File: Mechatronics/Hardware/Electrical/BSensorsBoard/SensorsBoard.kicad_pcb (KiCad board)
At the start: 2 copper layers, 49.8 x 13.7 mm, 10 parts, among them J1 Conn_01x01_Male, J2 Conn_01x01_Male, J3 Conn_01x01_Male, J4 Conn_01x01_Male, J5 Conn_01x01_Male, J6 Conn_01x01_Male, J7 Conn_01x01_Male, J8 Conn_01x01_Male, U1 ITR1802, U2 ITR1802

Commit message: Added changes
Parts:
- removed J5, J6, J7, J8: Conn_01x01_Male, Encoder:No3dmodelPinHeader_1x01_P2.54mm_Vertical
- removed U2: ITR1802, Encoder:itr8102
- added J1: Conn_01x01_Male, Encoder:No3dmodelPinHeader_1x01_P2.54mm_Vertical, F.Cu at (150.7, 120.2)
- added J1: Conn_01x01_Male, Encoder:No3dmodelPinHeader_1x01_P2.54mm_Vertical, F.Cu at (109.3, 76.7)
- added J1: Conn_01x01_Male, Encoder:No3dmodelPinHeader_1x01_P2.54mm_Vertical, F.Cu at (126.8, 92.9)
- added J1: Conn_01x01_Male, Encoder:No3dmodelPinHeader_1x01_P2.54mm_Vertical, F.Cu at (102.9, 92.9)
- added J1: Conn_01x01_Male, Encoder:No3dmodelPinHeader_1x01_P2.54mm_Vertical, F.Cu at (109.2, 104.0)
- added J1: Conn_01x01_Male, Encoder:No3dmodelPinHeader_1x01_P2.54mm_Vertical, F.Cu at (133.2, 104.0)
- added J1: Conn_01x01_Male, Encoder:No3dmodelPinHeader_1x01_P2.54mm_Vertical, F.Cu at (126.7, 120.2)
- added J1: Conn_01x01_Male, Encoder:No3dmodelPinHeader_1x01_P2.54mm_Vertical, F.Cu at (174.7, 120.2)
- added J1: Conn_01x01_Male, Encoder:No3dmodelPinHeader_1x01_P2.54mm_Vertical, F.Cu at (157.1, 104.0)
- added J1: Conn_01x01_Male, Encoder:No3dmodelPinHeader_1x01_P2.54mm_Vertical, F.Cu at (181.1, 104.0)
- added J1: Conn_01x01_Male, Encoder:No3dmodelPinHeader_1x01_P2.54mm_Vertical, F.Cu at (150.8, 92.9)
- added J1: Conn_01x01_Male, Encoder:No3dmodelPinHeader_1x01_P2.54mm_Vertical, F.Cu at (174.7, 92.9)
- added J1: Conn_01x01_Male, Encoder:No3dmodelPinHeader_1x01_P2.54mm_Vertical, F.Cu at (157.2, 76.7)
- added J1: Conn_01x01_Male, Encoder:No3dmodelPinHeader_1x01_P2.54mm_Vertical, F.Cu at (181.2, 76.7)
- added J1: Conn_01x01_Male, Encoder:No3dmodelPinHeader_1x01_P2.54mm_Vertical, F.Cu at (133.2, 76.7)
- added J2: Conn_01x01_Male, Encoder:No3dmodelPinHeader_1x01_P2.54mm_Vertical, F.Cu at (150.8, 96.4)
- added J2: Conn_01x01_Male, Encoder:No3dmodelPinHeader_1x01_P2.54mm_Vertical, F.Cu at (102.9, 96.4)
- added J2: Conn_01x01_Male, Encoder:No3dmodelPinHeader_1x01_P2.54mm_Vertical, F.Cu at (133.2, 73.2)
- added J2: Conn_01x01_Male, Encoder:No3dmodelPinHeader_1x01_P2.54mm_Vertical, F.Cu at (126.8, 96.4)
- added J2: Conn_01x01_Male, Encoder:No3dmodelPinHeader_1x01_P2.54mm_Vertical, F.Cu at (109.2, 100.5)
- added J2: Conn_01x01_Male, Encoder:No3dmodelPinHeader_1x01_P2.54mm_Vertical, F.Cu at (133.2, 100.5)
- added J2: Conn_01x01_Male, Encoder:No3dmodelPinHeader_1x01_P2.54mm_Vertical, F.Cu at (126.7, 123.7)
- added J2: Conn_01x01_Male, Encoder:No3dmodelPinHeader_1x01_P2.54mm_Vertical, F.Cu at (174.7, 123.7)
- added J2: Conn_01x01_Male, Encoder:No3dmodelPinHeader_1x01_P2.54mm_Vertical, F.Cu at (181.1, 100.5)
- added J2: Conn_01x01_Male, Encoder:No3dmodelPinHeader_1x01_P2.54mm_Vertical, F.Cu at (150.7, 123.7)
- added J2: Conn_01x01_Male, Encoder:No3dmodelPinHeader_1x01_P2.54mm_Vertical, F.Cu at (157.1, 100.5)
- added J2: Conn_01x01_Male, Encoder:No3dmodelPinHeader_1x01_P2.54mm_Vertical, F.Cu at (157.2, 73.2)
- added J2: Conn_01x01_Male, Encoder:No3dmodelPinHeader_1x01_P2.54mm_Vertical, F.Cu at (181.2, 73.2)
- added J2: Conn_01x01_Male, Encoder:No3dmodelPinHeader_1x01_P2.54mm_Vertical, F.Cu at (174.7, 96.4)
- added J2: Conn_01x01_Male, Encoder:No3dmodelPinHeader_1x01_P2.54mm_Vertical, F.Cu at (109.3, 73.2)
- added J3: Conn_01x01_Male, Encoder:No3dmodelPinHeader_1x01_P2.54mm_Vertical, F.Cu at (150.7, 76.8)
- added J3: Conn_01x01_Male, Encoder:No3dmodelPinHeader_1x01_P2.54mm_Vertical, F.Cu at (109.3, 92.8)
- added J3: Conn_01x01_Male, Encoder:No3dmodelPinHeader_1x01_P2.54mm_Vertical, F.Cu at (102.8, 76.8)
- added J3: Conn_01x01_Male, Encoder:No3dmodelPinHeader_1x01_P2.54mm_Vertical, F.Cu at (133.3, 92.8)
- added J3: Conn_01x01_Male, Encoder:No3dmodelPinHeader_1x01_P2.54mm_Vertical, F.Cu at (126.7, 104.1)
- added J3: Conn_01x01_Male, Encoder:No3dmodelPinHeader_1x01_P2.54mm_Vertical, F.Cu at (102.8, 104.1)
- added J3: Conn_01x01_Male, Encoder:No3dmodelPinHeader_1x01_P2.54mm_Vertical, F.Cu at (133.2, 120.1)
- added J3: Conn_01x01_Male, Encoder:No3dmodelPinHeader_1x01_P2.54mm_Vertical, F.Cu at (157.1, 120.1)
- added J3: Conn_01x01_Male, Encoder:No3dmodelPinHeader_1x01_P2.54mm_Vertical, F.Cu at (181.2, 92.8)
- added J3: Conn_01x01_Male, Encoder:No3dmodelPinHeader_1x01_P2.54mm_Vertical, F.Cu at (174.6, 104.1)
- added J3: Conn_01x01_Male, Encoder:No3dmodelPinHeader_1x01_P2.54mm_Vertical, F.Cu at (181.1, 120.1)
- added J3: Conn_01x01_Male, Encoder:No3dmodelPinHeader_1x01_P2.54mm_Vertical, F.Cu at (150.7, 104.1)
- added J3: Conn_01x01_Male, Encoder:No3dmodelPinHeader_1x01_P2.54mm_Vertical, F.Cu at (157.2, 92.8)
- added J3: Conn_01x01_Male, Encoder:No3dmodelPinHeader_1x01_P2.54mm_Vertical, F.Cu at (174.7, 76.8)
- added J3: Conn_01x01_Male, Encoder:No3dmodelPinHeader_1x01_P2.54mm_Vertical, F.Cu at (126.8, 76.8)
- added J4: Conn_01x01_Male, Encoder:No3dmodelPinHeader_1x01_P2.54mm_Vertical, F.Cu at (150.7, 73.2)
- added J4: Conn_01x01_Male, Encoder:No3dmodelPinHeader_1x01_P2.54mm_Vertical, F.Cu at (126.8, 73.2)
- added J4: Conn_01x01_Male, Encoder:No3dmodelPinHeader_1x01_P2.54mm_Vertical, F.Cu at (102.8, 73.2)
- added J4: Conn_01x01_Male, Encoder:No3dmodelPinHeader_1x01_P2.54mm_Vertical, F.Cu at (133.3, 96.4)
- added J4: Conn_01x01_Male, Encoder:No3dmodelPinHeader_1x01_P2.54mm_Vertical, F.Cu at (126.7, 100.5)
- added J4: Conn_01x01_Male, Encoder:No3dmodelPinHeader_1x01_P2.54mm_Vertical, F.Cu at (102.8, 100.5)
- added J4: Conn_01x01_Male, Encoder:No3dmodelPinHeader_1x01_P2.54mm_Vertical, F.Cu at (133.2, 123.7)
- added J4: Conn_01x01_Male, Encoder:No3dmodelPinHeader_1x01_P2.54mm_Vertical, F.Cu at (174.6, 100.5)
- added J4: Conn_01x01_Male, Encoder:No3dmodelPinHeader_1x01_P2.54mm_Vertical, F.Cu at (157.1, 123.7)
- added J4: Conn_01x01_Male, Encoder:No3dmodelPinHeader_1x01_P2.54mm_Vertical, F.Cu at (181.1, 123.7)
- added J4: Conn_01x01_Male, Encoder:No3dmodelPinHeader_1x01_P2.54mm_Vertical, F.Cu at (174.7, 73.2)
- added J4: Conn_01x01_Male, Encoder:No3dmodelPinHeader_1x01_P2.54mm_Vertical, F.Cu at (181.2, 96.4)
- added J4: Conn_01x01_Male, Encoder:No3dmodelPinHeader_1x01_P2.54mm_Vertical, F.Cu at (157.2, 96.4)
- added J4: Conn_01x01_Male, Encoder:No3dmodelPinHeader_1x01_P2.54mm_Vertical, F.Cu at (150.7, 100.5)
- added J4: Conn_01x01_Male, Encoder:No3dmodelPinHeader_1x01_P2.54mm_Vertical, F.Cu at (109.3, 96.4)
- added U1: ITR1802, Encoder:itr8102, F.Cu at (154.0, 87.8)
- added U1: ITR1802, Encoder:itr8102, F.Cu at (130.1, 81.8)
- added U1: ITR1802, Encoder:itr8102, F.Cu at (106.1, 81.8)
- added U1: ITR1802, Encoder:itr8102, F.Cu at (130.0, 87.8)
- added U1: ITR1802, Encoder:itr8102, F.Cu at (130.0, 109.1)
- added U1: ITR1802, Encoder:itr8102, F.Cu at (106.0, 109.1)
- added U1: ITR1802, Encoder:itr8102, F.Cu at (129.9, 115.1)
- added U1: ITR1802, Encoder:itr8102, F.Cu at (154.0, 81.8)
- added U1: ITR1802, Encoder:itr8102, F.Cu at (178.0, 81.8)
- added U1: ITR1802, Encoder:itr8102, F.Cu at (177.9, 87.8)
- added U1: ITR1802, Encoder:itr8102, F.Cu at (177.9, 109.1)
- added U1: ITR1802, Encoder:itr8102, F.Cu at (153.9, 115.1)
- added U1: ITR1802, Encoder:itr8102, F.Cu at (177.8, 115.1)
- added U1: ITR1802, Encoder:itr8102, F.Cu at (153.9, 109.1)
- added U1: ITR1802, Encoder:itr8102, F.Cu at (106.1, 87.8)
- moved J1 54.5 mm to (102.8, 120.2)
- moved J3 54.5 mm to (109.2, 120.1)
- moved U1 54.5 mm to (106.0, 115.1)
- moved J2 54.5 mm to (102.8, 123.7)
- moved J4 54.5 mm to (109.2, 123.7)
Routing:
- net (no net): track 0.00 -> 534.2 mm
- net Net-(J5-Pad1): track 9.53 -> 0.00 mm
- net Net-(J6-Pad1): track 9.22 -> 0.00 mm
- net Net-(J8-Pad1): track 9.10 -> 0.00 mm
- net Net-(J7-Pad1): track 8.42 -> 0.00 mm
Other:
- board size 49.8 x 13.7 mm -> 95.9 x 54.7 mm
- board text removed: "A"
- board text removed: "B"

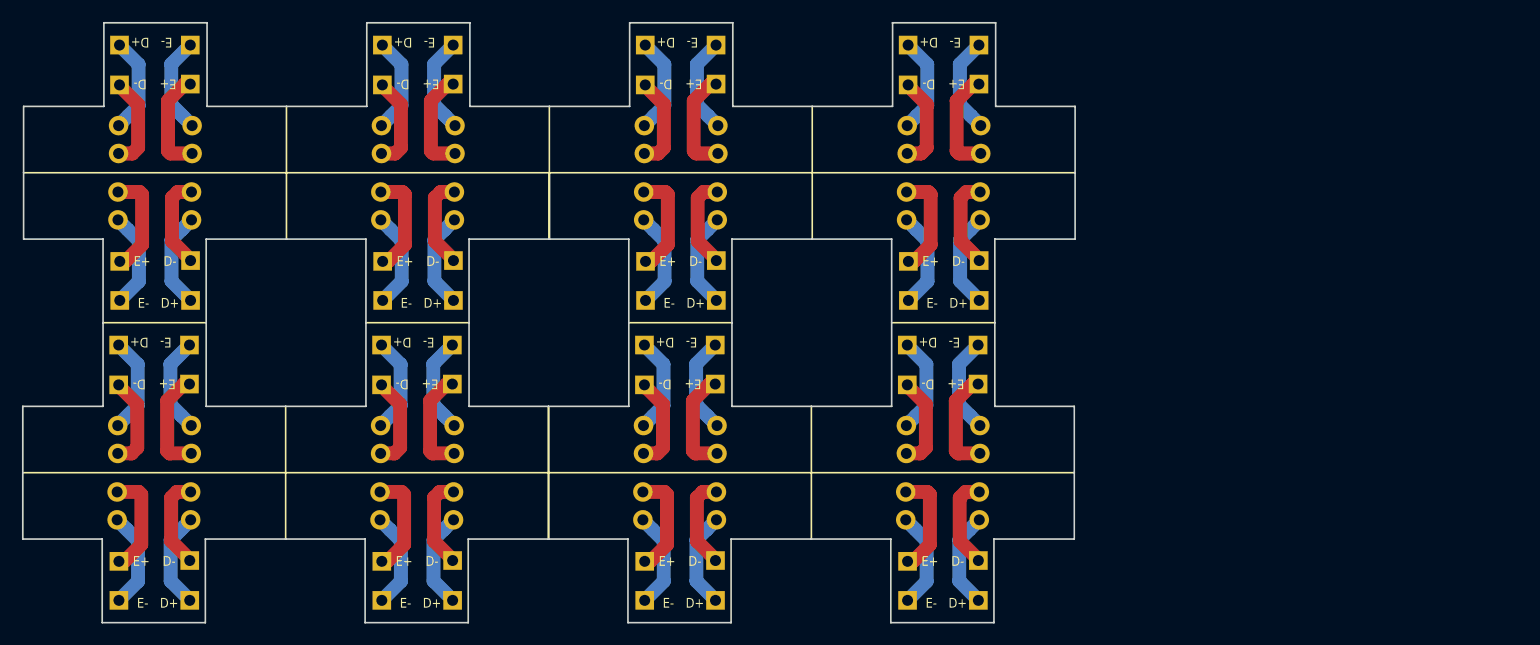
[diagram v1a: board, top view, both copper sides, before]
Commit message: Added SensorsBoard Gerbers
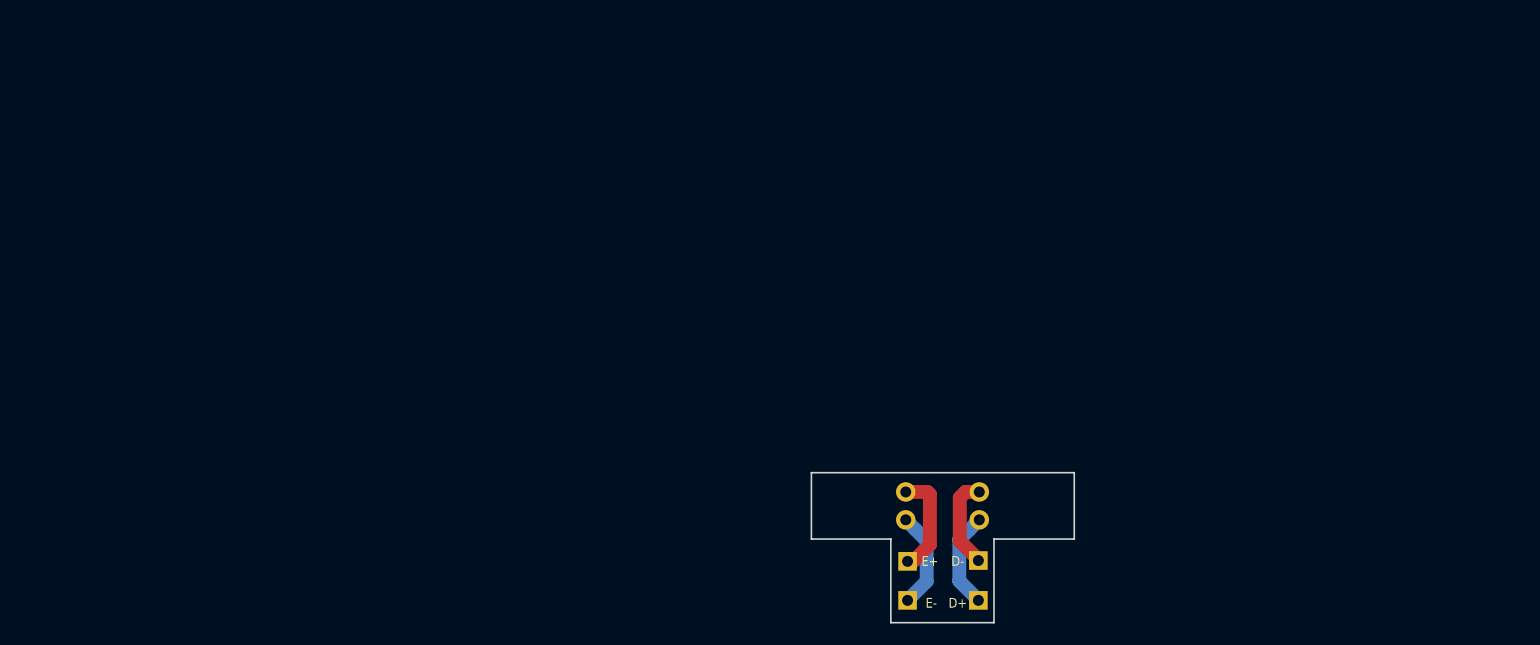
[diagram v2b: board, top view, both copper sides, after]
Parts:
- removed the J1 at (150.7, 120.2)
- removed the J1 at (109.3, 76.7)
- removed the J1 at (126.8, 92.9)
- removed the J1 at (102.9, 92.9)
- removed the J1 at (109.2, 104.0)
- removed the J1 at (133.2, 104.0)
- removed the J1 at (126.7, 120.2)
- removed the J1 at (102.8, 120.2)
- removed the J1 at (157.1, 104.0)
- removed the J1 at (181.1, 104.0)
- removed the J1 at (150.8, 92.9)
- removed the J1 at (174.7, 92.9)
- removed the J1 at (157.2, 76.7)
- removed the J1 at (181.2, 76.7)
- removed the J1 at (133.2, 76.7)
- removed the J2 at (150.8, 96.4)
- removed the J2 at (102.9, 96.4)
- removed the J2 at (133.2, 73.2)
- removed the J2 at (126.8, 96.4)
- removed the J2 at (109.2, 100.5)
- removed the J2 at (133.2, 100.5)
- removed the J2 at (126.7, 123.7)
- removed the J2 at (102.8, 123.7)
- removed the J2 at (181.1, 100.5)
- removed the J2 at (150.7, 123.7)
- removed the J2 at (157.1, 100.5)
- removed the J2 at (157.2, 73.2)
- removed the J2 at (181.2, 73.2)
- removed the J2 at (174.7, 96.4)
- removed the J2 at (109.3, 73.2)
- removed the J3 at (150.7, 76.8)
- removed the J3 at (109.3, 92.8)
- removed the J3 at (102.8, 76.8)
- removed the J3 at (133.3, 92.8)
- removed the J3 at (126.7, 104.1)
- removed the J3 at (102.8, 104.1)
- removed the J3 at (133.2, 120.1)
- removed the J3 at (109.2, 120.1)
- removed the J3 at (157.1, 120.1)
- removed the J3 at (181.2, 92.8)
- removed the J3 at (174.6, 104.1)
- removed the J3 at (150.7, 104.1)
- removed the J3 at (157.2, 92.8)
- removed the J3 at (174.7, 76.8)
- removed the J3 at (126.8, 76.8)
- removed the J4 at (150.7, 73.2)
- removed the J4 at (126.8, 73.2)
- removed the J4 at (102.8, 73.2)
- removed the J4 at (133.3, 96.4)
- removed the J4 at (126.7, 100.5)
- removed the J4 at (102.8, 100.5)
- removed the J4 at (133.2, 123.7)
- removed the J4 at (109.2, 123.7)
- removed the J4 at (174.6, 100.5)
- removed the J4 at (157.1, 123.7)
- removed the J4 at (174.7, 73.2)
- removed the J4 at (181.2, 96.4)
- removed the J4 at (157.2, 96.4)
- removed the J4 at (150.7, 100.5)
- removed the J4 at (109.3, 96.4)
- removed the U1 at (154.0, 87.8)
- removed the U1 at (130.1, 81.8)
- removed the U1 at (106.1, 81.8)
- removed the U1 at (130.0, 87.8)
- removed the U1 at (130.0, 109.1)
- removed the U1 at (106.0, 109.1)
- removed the U1 at (129.9, 115.1)
- removed the U1 at (106.0, 115.1)
- removed the U1 at (154.0, 81.8)
- removed the U1 at (178.0, 81.8)
- removed the U1 at (177.9, 87.8)
- removed the U1 at (177.9, 109.1)
- removed the U1 at (153.9, 115.1)
- removed the U1 at (153.9, 109.1)
- removed the U1 at (106.1, 87.8)
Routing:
- net (no net): track 534.2 -> 35.6 mm
- net Net-(J1-Pad1): track 9.53 -> 0.00 mm
- net Net-(J2-Pad1): track 8.85 -> 0.00 mm
- net Net-(J4-Pad1): track 8.81 -> 0.00 mm
- net Net-(J3-Pad1): track 8.42 -> 0.00 mm
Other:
- board size 95.9 x 54.7 mm -> 24 x 13.7 mm

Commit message: Changes
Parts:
- added J1: Conn_01x01_Male, Encoder:No3dmodelPinHeader_1x01_P2.54mm_Vertical, F.Cu at (222.3, 120.2)
- added J1: Conn_01x01_Male, Encoder:No3dmodelPinHeader_1x01_P2.54mm_Vertical, F.Cu at (228.7, 100.0)
- added J1: Conn_01x01_Male, Encoder:No3dmodelPinHeader_1x01_P2.54mm_Vertical, F.Cu at (210.4, 120.2)
- added J1: Conn_01x01_Male, Encoder:No3dmodelPinHeader_1x01_P2.54mm_Vertical, F.Cu at (216.7, 100.0)
- added J1: Conn_01x01_Male, Encoder:No3dmodelPinHeader_1x01_P2.54mm_Vertical, F.Cu at (198.5, 120.2)
- added J1: Conn_01x01_Male, Encoder:No3dmodelPinHeader_1x01_P2.54mm_Vertical, F.Cu at (204.8, 100.0)
- added J1: Conn_01x01_Male, Encoder:No3dmodelPinHeader_1x01_P2.54mm_Vertical, F.Cu at (186.6, 120.2)
- added J1: Conn_01x01_Male, Encoder:No3dmodelPinHeader_1x01_P2.54mm_Vertical, F.Cu at (192.9, 100.0)
- added J1: Conn_01x01_Male, Encoder:No3dmodelPinHeader_1x01_P2.54mm_Vertical, F.Cu at (181.0, 100.0)
- added J2: Conn_01x01_Male, Encoder:No3dmodelPinHeader_1x01_P2.54mm_Vertical, F.Cu at (228.7, 96.5)
- added J2: Conn_01x01_Male, Encoder:No3dmodelPinHeader_1x01_P2.54mm_Vertical, F.Cu at (222.3, 123.7)
- added J2: Conn_01x01_Male, Encoder:No3dmodelPinHeader_1x01_P2.54mm_Vertical, F.Cu at (216.7, 96.5)
- added J2: Conn_01x01_Male, Encoder:No3dmodelPinHeader_1x01_P2.54mm_Vertical, F.Cu at (210.4, 123.7)
- added J2: Conn_01x01_Male, Encoder:No3dmodelPinHeader_1x01_P2.54mm_Vertical, F.Cu at (204.8, 96.5)
- added J2: Conn_01x01_Male, Encoder:No3dmodelPinHeader_1x01_P2.54mm_Vertical, F.Cu at (198.5, 123.7)
- added J2: Conn_01x01_Male, Encoder:No3dmodelPinHeader_1x01_P2.54mm_Vertical, F.Cu at (186.6, 123.7)
- added J2: Conn_01x01_Male, Encoder:No3dmodelPinHeader_1x01_P2.54mm_Vertical, F.Cu at (192.9, 96.5)
- added J2: Conn_01x01_Male, Encoder:No3dmodelPinHeader_1x01_P2.54mm_Vertical, F.Cu at (181.0, 96.5)
- added J3: Conn_01x01_Male, Encoder:No3dmodelPinHeader_1x01_P2.54mm_Vertical, F.Cu at (222.2, 100.1)
- added J3: Conn_01x01_Male, Encoder:No3dmodelPinHeader_1x01_P2.54mm_Vertical, F.Cu at (228.8, 120.1)
- added J3: Conn_01x01_Male, Encoder:No3dmodelPinHeader_1x01_P2.54mm_Vertical, F.Cu at (210.3, 100.1)
- added J3: Conn_01x01_Male, Encoder:No3dmodelPinHeader_1x01_P2.54mm_Vertical, F.Cu at (216.8, 120.1)
- added J3: Conn_01x01_Male, Encoder:No3dmodelPinHeader_1x01_P2.54mm_Vertical, F.Cu at (198.4, 100.1)
- added J3: Conn_01x01_Male, Encoder:No3dmodelPinHeader_1x01_P2.54mm_Vertical, F.Cu at (204.9, 120.1)
- added J3: Conn_01x01_Male, Encoder:No3dmodelPinHeader_1x01_P2.54mm_Vertical, F.Cu at (186.5, 100.1)
- added J3: Conn_01x01_Male, Encoder:No3dmodelPinHeader_1x01_P2.54mm_Vertical, F.Cu at (193.0, 120.1)
- added J3: Conn_01x01_Male, Encoder:No3dmodelPinHeader_1x01_P2.54mm_Vertical, F.Cu at (174.5, 100.1)
- added J4: Conn_01x01_Male, Encoder:No3dmodelPinHeader_1x01_P2.54mm_Vertical, F.Cu at (228.8, 123.7)
- added J4: Conn_01x01_Male, Encoder:No3dmodelPinHeader_1x01_P2.54mm_Vertical, F.Cu at (222.2, 96.5)
- added J4: Conn_01x01_Male, Encoder:No3dmodelPinHeader_1x01_P2.54mm_Vertical, F.Cu at (216.8, 123.7)
- added J4: Conn_01x01_Male, Encoder:No3dmodelPinHeader_1x01_P2.54mm_Vertical, F.Cu at (210.3, 96.5)
- added J4: Conn_01x01_Male, Encoder:No3dmodelPinHeader_1x01_P2.54mm_Vertical, F.Cu at (204.9, 123.7)
- added J4: Conn_01x01_Male, Encoder:No3dmodelPinHeader_1x01_P2.54mm_Vertical, F.Cu at (198.4, 96.5)
- added J4: Conn_01x01_Male, Encoder:No3dmodelPinHeader_1x01_P2.54mm_Vertical, F.Cu at (186.5, 96.5)
- added J4: Conn_01x01_Male, Encoder:No3dmodelPinHeader_1x01_P2.54mm_Vertical, F.Cu at (193.0, 123.7)
- added J4: Conn_01x01_Male, Encoder:No3dmodelPinHeader_1x01_P2.54mm_Vertical, F.Cu at (174.5, 96.5)
- added U1: ITR1802, Encoder:itr8102, F.Cu at (225.5, 115.1)
- added U1: ITR1802, Encoder:itr8102, F.Cu at (225.5, 105.1)
- added U1: ITR1802, Encoder:itr8102, F.Cu at (213.6, 115.1)
- added U1: ITR1802, Encoder:itr8102, F.Cu at (213.6, 105.1)
- added U1: ITR1802, Encoder:itr8102, F.Cu at (201.7, 115.1)
- added U1: ITR1802, Encoder:itr8102, F.Cu at (201.6, 105.1)
- added U1: ITR1802, Encoder:itr8102, F.Cu at (189.7, 105.1)
- added U1: ITR1802, Encoder:itr8102, F.Cu at (189.7, 115.1)
- added U1: ITR1802, Encoder:itr8102, F.Cu at (177.8, 105.1)
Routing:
- net (no net): track 35.6 -> 356.1 mm
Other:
- board size 24 x 13.7 mm -> 57 x 31.3 mm

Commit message: Changes
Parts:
- removed the J1 at (222.3, 120.2)
- removed the J1 at (228.7, 100.0)
- removed the J1 at (210.4, 120.2)
- removed the J1 at (216.7, 100.0)
- removed the J1 at (198.5, 120.2)
- removed the J1 at (204.8, 100.0)
- removed the J1 at (186.6, 120.2)
- removed the J1 at (192.9, 100.0)
- removed the J1 at (181.0, 100.0)
- removed the J2 at (228.7, 96.5)
- removed the J2 at (222.3, 123.7)
- removed the J2 at (216.7, 96.5)
- removed the J2 at (210.4, 123.7)
- removed the J2 at (204.8, 96.5)
- removed the J2 at (198.5, 123.7)
- removed the J2 at (186.6, 123.7)
- removed the J2 at (192.9, 96.5)
- removed the J2 at (181.0, 96.5)
- removed the J3 at (222.2, 100.1)
- removed the J3 at (228.8, 120.1)
- removed the J3 at (210.3, 100.1)
- removed the J3 at (216.8, 120.1)
- removed the J3 at (198.4, 100.1)
- removed the J3 at (204.9, 120.1)
- removed the J3 at (186.5, 100.1)
- removed the J3 at (193.0, 120.1)
- removed the J3 at (174.5, 100.1)
- removed the J4 at (228.8, 123.7)
- removed the J4 at (222.2, 96.5)
- removed the J4 at (216.8, 123.7)
- removed the J4 at (210.3, 96.5)
- removed the J4 at (204.9, 123.7)
- removed the J4 at (198.4, 96.5)
- removed the J4 at (186.5, 96.5)
- removed the J4 at (193.0, 123.7)
- removed the J4 at (174.5, 96.5)
- removed the U1 at (225.5, 115.1)
- removed the U1 at (225.5, 105.1)
- removed the U1 at (213.6, 115.1)
- removed the U1 at (213.6, 105.1)
- removed the U1 at (201.7, 115.1)
- removed the U1 at (201.6, 105.1)
- removed the U1 at (189.7, 105.1)
- removed the U1 at (189.7, 115.1)
- removed the U1 at (177.8, 105.1)
- added J1: Conn_01x01_Male, Encoder:No3dmodelPinHeader_1x01_P2.54mm_Vertical, F.Cu at (181.0, 90.8)
- added J2: Conn_01x01_Male, Encoder:No3dmodelPinHeader_1x01_P2.54mm_Vertical, F.Cu at (181.0, 87.2)
- added J3: Conn_01x01_Male, Encoder:No3dmodelPinHeader_1x01_P2.54mm_Vertical, F.Cu at (174.5, 90.8)
- added J4: Conn_01x01_Male, Encoder:No3dmodelPinHeader_1x01_P2.54mm_Vertical, F.Cu at (174.5, 87.2)
- added U1: ITR1802, Encoder:itr8102, F.Cu at (177.8, 95.8)
- moved J1 0.08 mm to (174.7, 120.1)
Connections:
- J1 pad 1: (no net) -> Net-(J1-Pad1)
- J2 pad 1: (no net) -> Net-(J2-Pad1)
- J3 pad 1: (no net) -> Net-(J3-Pad1)
- J4 pad 1: (no net) -> Net-(J4-Pad1)
- U1 pad 1: (no net) -> Net-(J1-Pad1)
- U1 pad 2: (no net) -> Net-(J2-Pad1)
- U1 pad 3: (no net) -> Net-(J4-Pad1)
- U1 pad 4: (no net) -> Net-(J3-Pad1)
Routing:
- net (no net): track 356.1 -> 36.6 mm
- net Net-(J2-Pad1): track 0.00 -> 9.79 mm
- net Net-(J1-Pad1): track 0.00 -> 9.53 mm
- net Net-(J4-Pad1): track 0.00 -> 8.81 mm
- net Net-(J3-Pad1): track 0.00 -> 8.42 mm
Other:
- board size 57 x 31.3 mm -> 9.4 x 40.7 mm
- net class Default: clearance 0.254 -> 0.127; trace_width 0.254 -> 0.127
- rule trace_clearance: 0.254 -> 0.127
- rule trace_min: 0.254 -> 0.127
